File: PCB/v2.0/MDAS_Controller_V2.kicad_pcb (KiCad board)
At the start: 4 copper layers, 66.7 x 102.9 mm, 96 parts, among them J2 DB9_Male, J3 DB15_Male, Q1 DTC114E, Q2 DTC114E, Q3 DTC114E, SW1 SW_DIP_x04, T2 TestPoint, T5 TestPoint, U1 TM4C123GH6PM, U10 TPS70933DBVT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

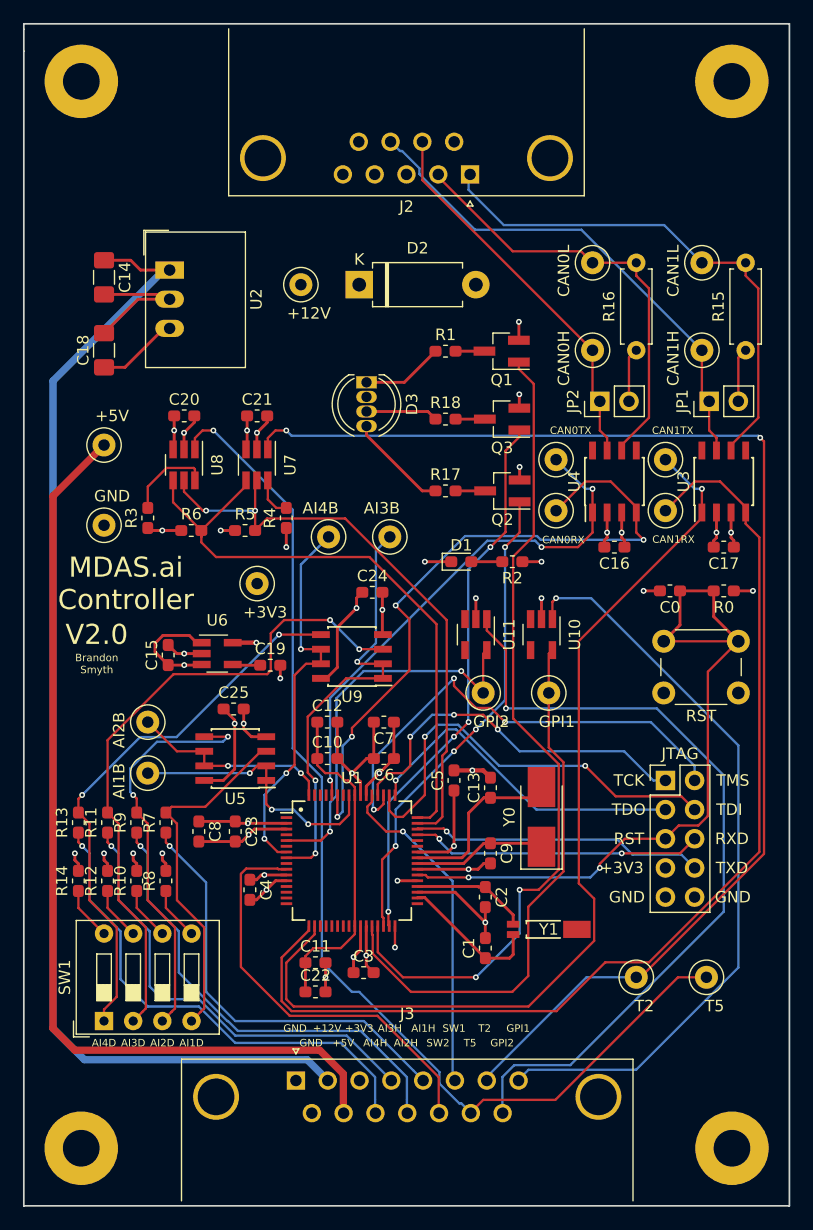
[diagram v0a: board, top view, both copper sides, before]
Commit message: Redesign routing
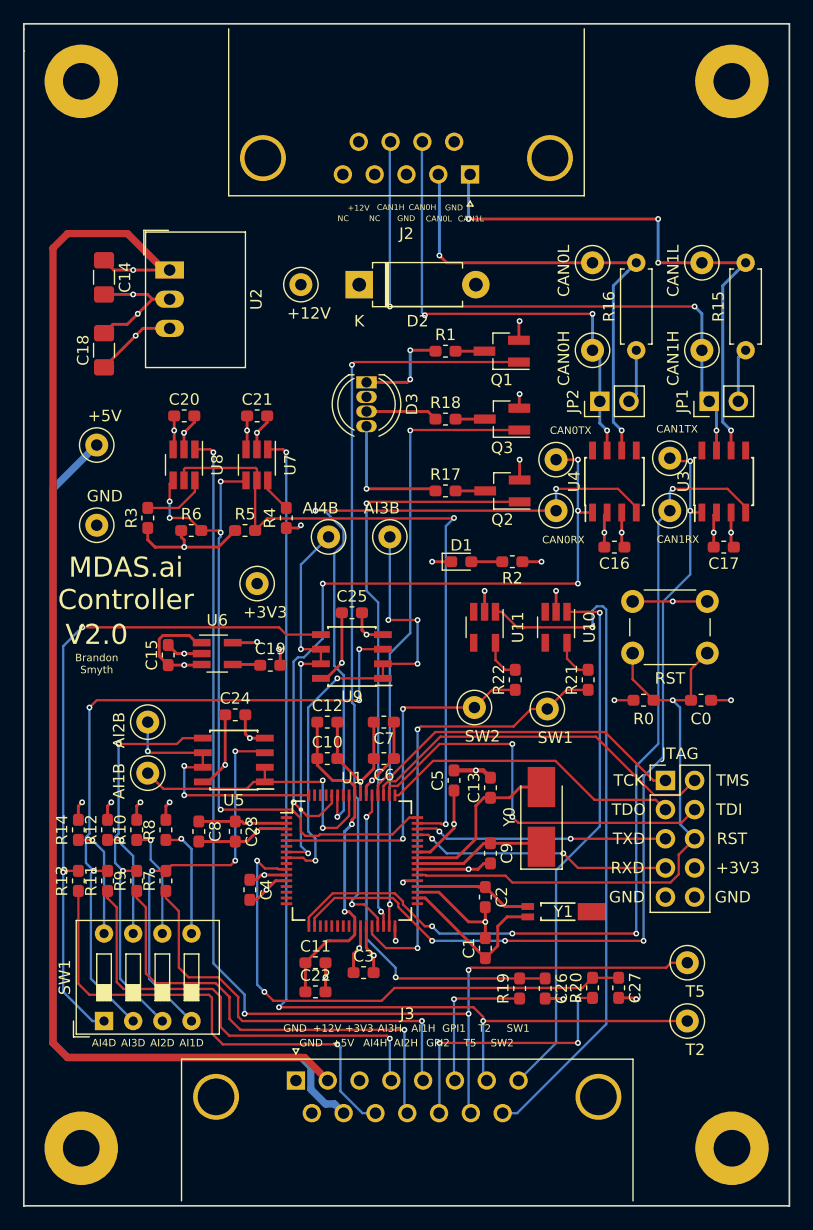
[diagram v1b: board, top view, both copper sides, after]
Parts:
- removed GPI2: TestPoint, TestPoint:TestPoint_Loop_D1.80mm_Drill1.0mm_Beaded
- added C26: 0.01uF, Capacitor_SMD:C_0603_1608Metric_Pad1.05x0.95mm_HandSolder, F.Cu at (160.3, 117.8)
- added C27: 0.01uF, Capacitor_SMD:C_0603_1608Metric_Pad1.05x0.95mm_HandSolder, F.Cu at (166.7, 117.8)
- added R19: 1k, Resistor_SMD:R_0603_1608Metric_Pad1.05x0.95mm_HandSolder, F.Cu at (158.1, 117.8)
- added R20: 1k, Resistor_SMD:R_0603_1608Metric_Pad1.05x0.95mm_HandSolder, F.Cu at (164.5, 117.8)
- added R21: 1k, Resistor_SMD:R_0603_1608Metric_Pad1.05x0.95mm_HandSolder, F.Cu at (164.1, 90.9)
- added R22: 1k, Resistor_SMD:R_0603_1608Metric_Pad1.05x0.95mm_HandSolder, F.Cu at (157.7, 90.9)
- added SW2: TestPoint, TestPoint:TestPoint_Loop_D1.80mm_Drill1.0mm_Beaded, F.Cu at (154.2, 93.3)
- moved C24 16.0 mm to (133.3, 94.0)
- moved C25 13.3 mm to (143.5, 85.1)
- moved RST 12.2 mm to (168.0, 84.1), turned to 0 degrees
- moved R0 11.8 mm to (168.9, 92.7), turned to 0 degrees
- moved C0 9.90 mm to (173.9, 92.7), turned to 0 degrees
- moved T2 5.85 mm to (172.7, 120.7)
- moved R11 5.08 mm to (122.2, 108.4)
- moved R13 5.08 mm to (119.7, 108.4)
- moved R7 5.08 mm to (127.3, 108.4)
- moved R9 5.08 mm to (124.8, 108.4)
- moved R10 4.44 mm to (124.8, 104.0)
- moved R12 4.44 mm to (122.2, 104.0)
- moved R14 4.44 mm to (119.7, 104.0)
- moved R8 4.44 mm to (127.3, 104.0)
- moved T5 2.09 mm to (172.7, 115.6)
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- renumbered GPI1 to SW1
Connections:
- J2 pad 6: Net-(J2-Pad6) -> GND
- J3 pad 13: SW2 -> GPI2
- J3 pad 15: GPI2 -> SW2
- J3 pad 6: SW1 -> GPI1
- J3 pad 8: GPI1 -> SW1
- JTAG pad 5: RST -> TXD
- JTAG pad 6: RXD -> RST
- JTAG pad 7: +3V3 -> RXD
- JTAG pad 8: TXD -> +3V3
- SW1 pad 1: GPI1P -> SW1P
- U1 pad 10: SW2 -> Net-(C27-Pad1)
- U1 pad 28: GPI1P -> SW1P
- U1 pad 5: GPI2P -> SW2P
- U1 pad 53: SW1 -> Net-(C26-Pad1)
- U10 pad 1: GPI1 -> SW1
- U10 pad 5: GPI1P -> Net-(R21-Pad2)
- U11 pad 1: GPI2 -> SW2
- U11 pad 5: GPI2P -> Net-(R22-Pad2)
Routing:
- net GPI1: track 65.7 -> 12.9 mm
- net GPI1P: track 48.2 -> 0.00 mm
- net GPI2: track 70.1 -> 23.3 mm, vias 1 -> 3
- net Net-(C27-Pad1): track 0.00 -> 46.6 mm, vias 0 -> 2
- net SW1P: track 0.00 -> 40.5 mm, vias 0 -> 2
- net GPI2P: track 34.4 -> 0.00 mm, vias 2 -> 0
- net SW2P: track 0.00 -> 32.0 mm, vias 0 -> 2
- net Net-(C26-Pad1): track 0.00 -> 30.2 mm, vias 0 -> 2
- net SW2: track 36.6 -> 60.9 mm, vias 0 -> 1
- net T2: track 113.3 -> 91.9 mm, vias 2 -> 3
- net SW1: track 28.8 -> 46.7 mm
- net CAN0TX: track 45.9 -> 61.8 mm, vias 3 -> 5
- net CAN1RX: track 94.7 -> 79.3 mm, vias 0 -> 4
- net Net-(R13-Pad2): track 48.2 -> 59.5 mm
- net RST: track 63.7 -> 52.7 mm, vias 2 -> 1
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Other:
- board text added: "CAN0H"
- board text added: "CAN0L"
- board text added: "CAN1H"
- board text added: "CAN1L"
- board text added: "NC"

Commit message: Minor changes before Hughes manufactures
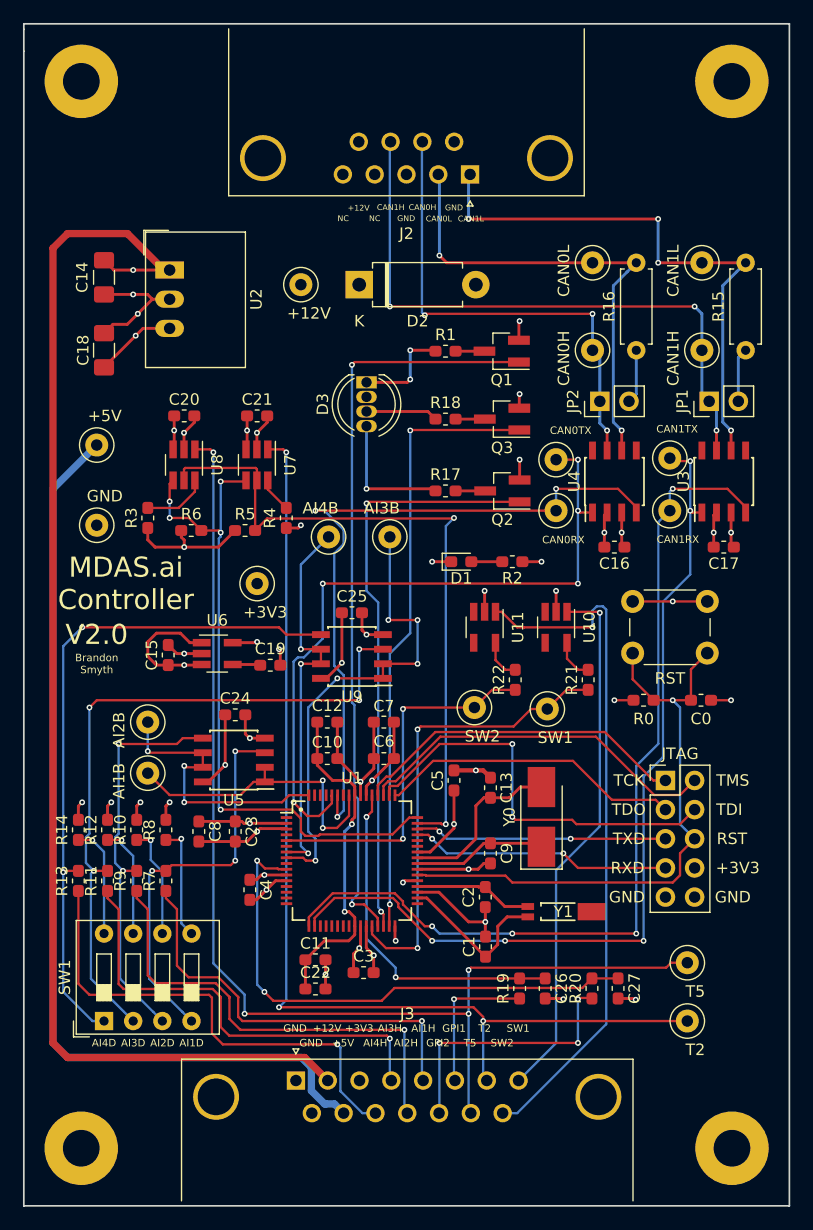
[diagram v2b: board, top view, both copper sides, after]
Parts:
- moved C22 0.25 mm to (140.3, 117.9)
- moved C11 0.25 mm to (140.3, 115.3)
- moved C1 0.13 mm to (155.1, 114.2)
- moved C27 0.07 mm to (166.7, 117.8)
- moved R20 0.07 mm to (164.4, 117.8)
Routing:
- net +5V: track 116.3 -> 118.5 mm
- net AI2B: track 23.7 -> 24.7 mm
- net AI1B: track 26.0 -> 26.6 mm
